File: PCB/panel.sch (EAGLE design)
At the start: 20 parts, among them U1 22PINHEADER22PINHEADER, U2 22PINHEADER22PINHEADER

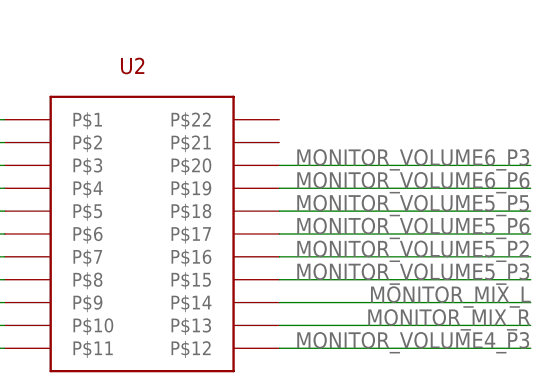
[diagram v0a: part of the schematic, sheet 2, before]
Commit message: Add switch and analog selectors
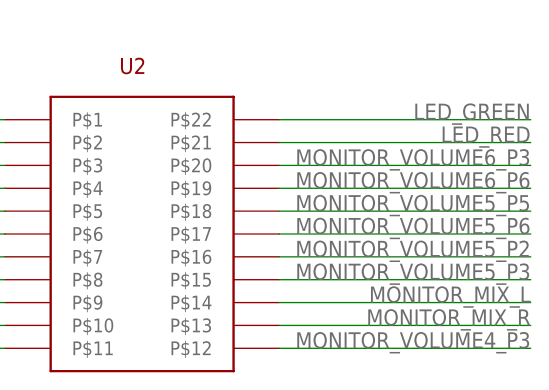
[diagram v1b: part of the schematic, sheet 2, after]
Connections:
- new net LED_GREEN: U2.P$22
- new net LED_RED: U2.P$21
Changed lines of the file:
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@@
+</segment>
+</net>
+<net name="LED_RED" class="0">
+<segment>
+<wire x1="264.16" y1="144.78" x2="292.1" y2="144.78" width="0.1524" layer="91"/>
+<label x="292.1" y="144.78" size="1.778" layer="95" rot="MR0"/>
+<pinref part="U2" gate="G$1" pin="P$21"/>
+</segment>
+</net>
+<net name="LED_GREEN" class="0">
+<segment>
+<wire x1="264.16" y1="147.32" x2="292.1" y2="147.32" width="0.1524" layer="91"/>
+<label x="292.1" y="147.32" size="1.778" layer="95" rot="MR0"/>
+<pinref part="U2" gate="G$1" pin="P$22"/>
 </segment>
 </net>

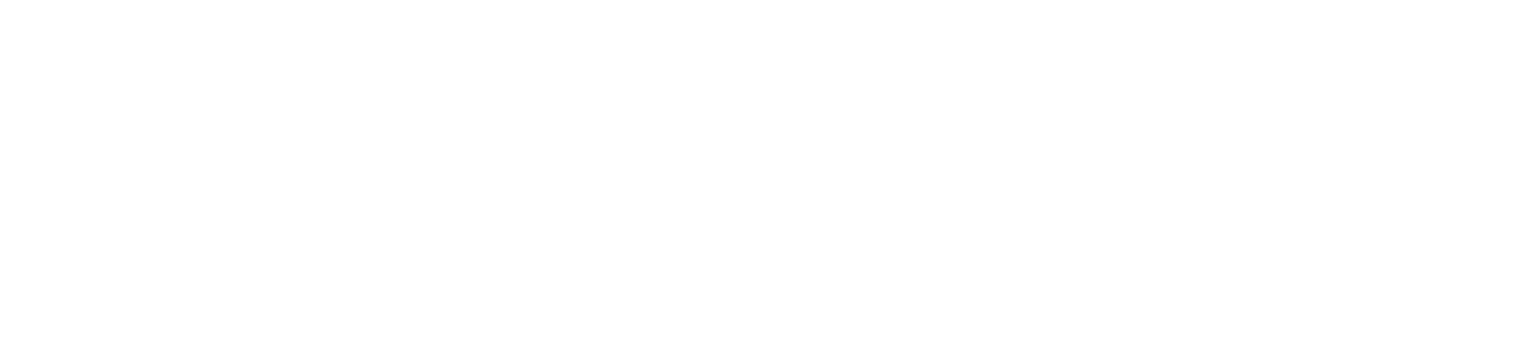
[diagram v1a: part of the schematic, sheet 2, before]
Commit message: Updating to 2 layer
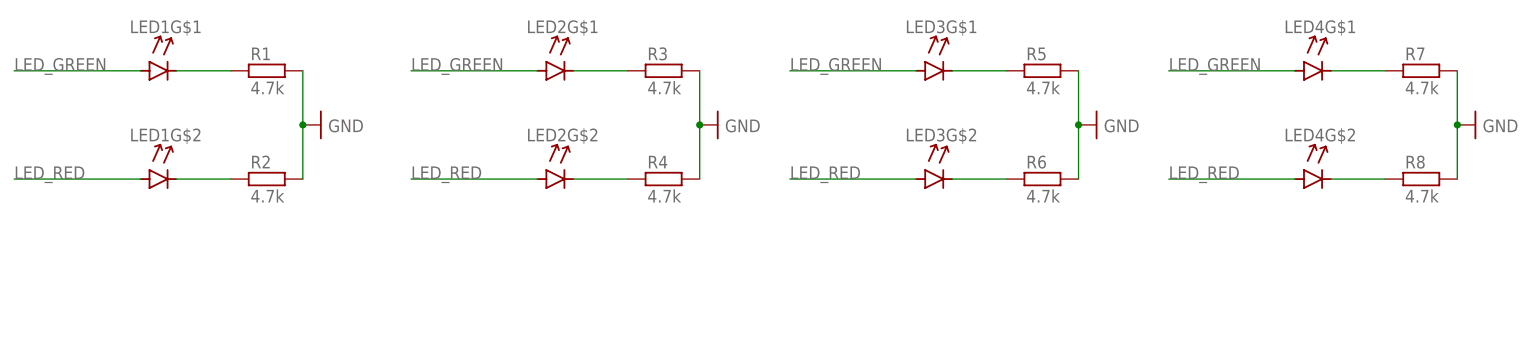
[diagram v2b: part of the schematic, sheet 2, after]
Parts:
- added LED1, LED2, LED3, LED4: DUAL_LEDDUAL_LED, lib:DUAL_LEDDUAL_LED
- added R1, R2, R3, R4, R5, R6, R7, R8: 4.7k, lib:RESISTOR
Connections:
- new net N$1: LED1G$1.C, R1.1
- new net N$2: LED1G$2.C, R2.1
- new net N$3: LED2G$1.C, R3.1
- new net N$4: LED2G$2.C, R4.1
- new net N$5: LED3G$1.C, R5.1
- new net N$6: LED3G$2.C, R6.1
- new net N$7: LED4G$1.C, R7.1
- new net N$8: LED4G$2.C, R8.1
- net GND: now also R1.2, R2.2, R3.2, R4.2, R5.2, R6.2, R7.2, R8.2
- net LED_GREEN: now also LED1G$1.A, LED2G$1.A, LED3G$1.A, LED4G$1.A
- net LED_RED: now also LED1G$2.A, LED2G$2.A, LED3G$2.A, LED4G$2.A
